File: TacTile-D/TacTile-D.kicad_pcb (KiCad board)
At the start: 2 copper layers, 60 x 60 mm, 19 parts, among them J1 Conn_01x06, J2 Conn_01x06, J3 Conn_01x06, J4 Conn_01x06, J5 Conn_01x04, J6 Conn_01x05, J7 Conn_01x02, J8 Conn_01x02, U1 74LVC2G08, U10 74LVC1G373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

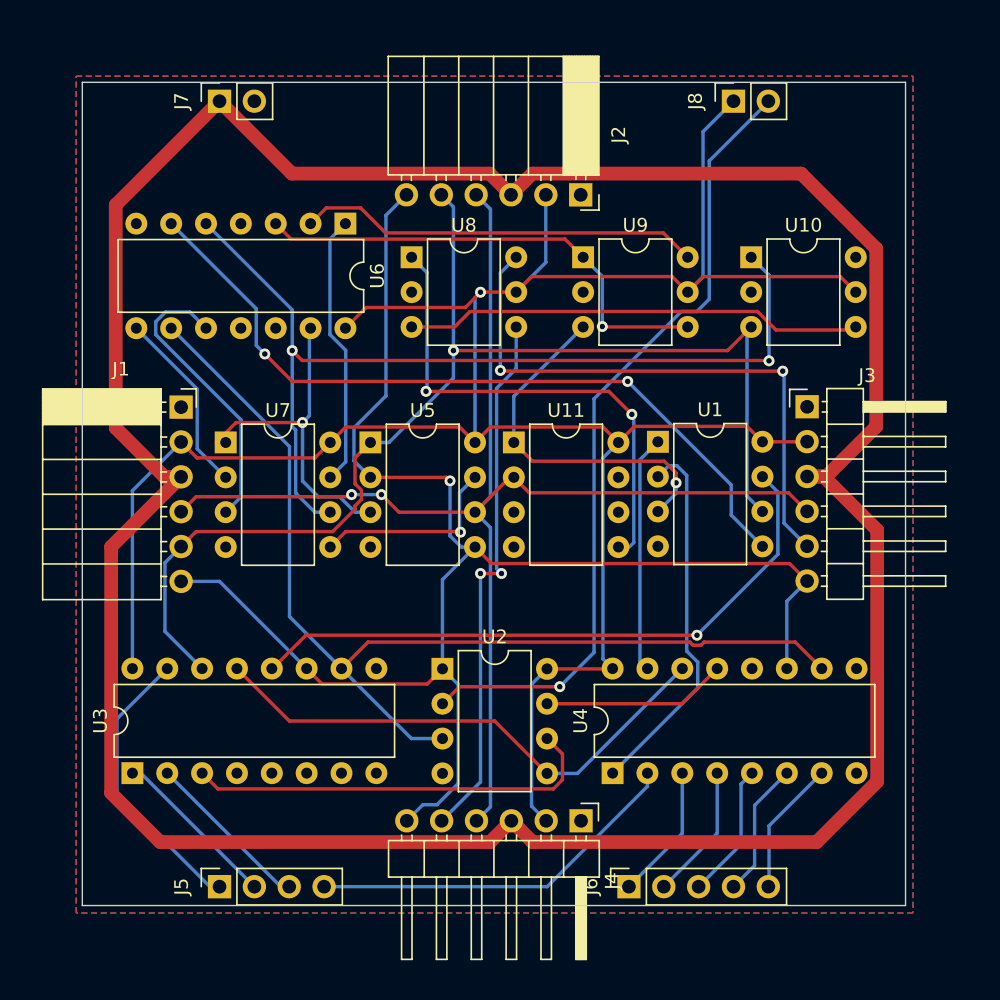
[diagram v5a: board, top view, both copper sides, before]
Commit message: Finished enlarging pins on C, D, L1, L2
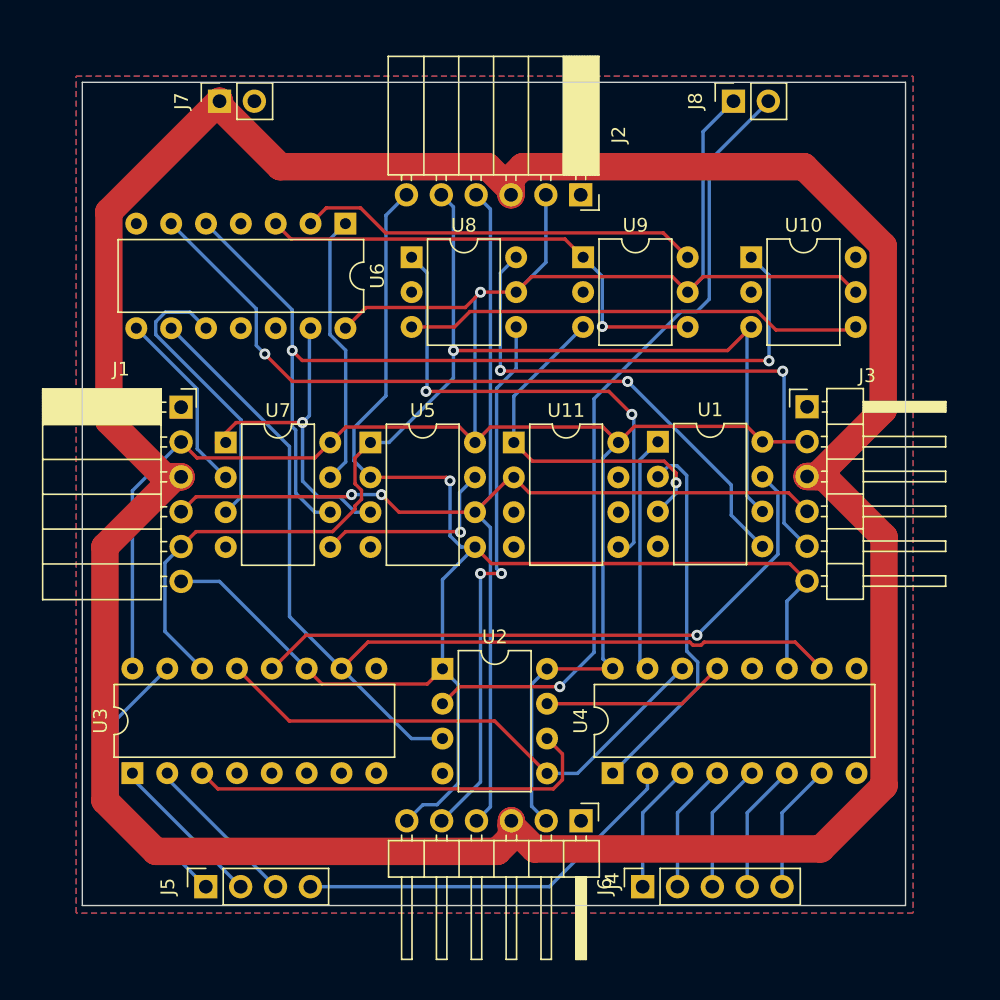
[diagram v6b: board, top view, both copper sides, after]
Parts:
- moved J5 1.00 mm to (34.0, 83.6)
- moved J6 1.00 mm to (65.8, 83.6)
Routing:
- net VIN: track 216.9 -> 223.3 mm
- net LS3: track 27.6 -> 28.7 mm
- net LS0: track 21.0 -> 20.1 mm
- net LS1: track 12.3 -> 11.5 mm
- net LS2: track 12.3 -> 11.5 mm
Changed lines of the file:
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@@
   )
   (footprint "Connector_PinSocket_2.54mm:PinSocket_1x04_P2.54mm_Vertical" (layer "F.Cu")
-    (at 35 83.625 90)
+    (at 34 83.625 90)
     (descr "Through hole straight socket strip, 1x04, 2.54mm pitch, single row (from Kicad 4.0.7), script generated")
     (tags "Through hole socket strip THT 1x04 2.54mm single row")
@@
   )
   (footprint "Connector_PinSocket_2.54mm:PinSocket_1x05_P2.54mm_Vertical" (layer "F.Cu")
-    (at 64.84 83.625 90)
+    (at 65.84 83.625 90)
     (descr "Through hole straight socket strip, 1x05, 2.54mm pitch, single row (from Kicad 4.0.7), script generated")
     (tags "Through hole socket strip THT 1x05 2.54mm single row")
@@
   (segment (start 53.73 78.825) (end 54.7455 77.8095) (width 0.25) (layer "B.Cu") (net 3))
   (segment (start 53.705 33.2) (end 54.745 34.24) (width 0.25) (layer "B.Cu") (net 3))
-  (segment (start 82.87 50.08) (end 79.22 53.73) (width 1) (layer "F.Cu") (net 4))
-  (segment (start 27.435 33.94) (end 35 26.375) (width 1) (layer "F.Cu") (net 4))
-  (segment (start 82.87 37.128679) (end 82.87 50.08) (width 1) (layer "F.Cu") (net 4))
-  (segment (start 77.825 53.73) (end 79.027081 53.73) (width 1) (layer "F.Cu") (net 4))
-  (segment (start 79.22 53.73) (end 77.825 53.73) (width 1) (layer "F.Cu") (net 4))
-  (segment (start 27.435 50.192081) (end 27.435 33.94) (width 1) (layer "F.Cu") (net 4))
-  (segment (start 56.245 33.2) (end 57.795 31.65) (width 1) (layer "F.Cu") (net 4))
-  (segment (start 54.695 31.65) (end 40.275 31.65) (width 1) (layer "F.Cu") (net 4))
-  (segment (start 54.72 80.375) (end 30.675 80.375) (width 1) (layer "F.Cu") (net 4))
-  (segment (start 57.795 31.65) (end 77.391321 31.65) (width 1) (layer "F.Cu") (net 4))
-  (segment (start 82.93 57.632919) (end 82.93 75.971321) (width 1) (layer "F.Cu") (net 4))
-  (segment (start 32.2 53.755) (end 30.997919 53.755) (width 1) (layer "F.Cu") (net 4))
-  (segment (start 56.245 33.2) (end 54.695 31.65) (width 1) (layer "F.Cu") (net 4))
-  (segment (start 79.027081 53.73) (end 82.93 57.632919) (width 1) (layer "F.Cu") (net 4))
-  (segment (start 30.675 80.375) (end 27.1 76.8) (width 1) (layer "F.Cu") (net 4))
-  (segment (start 78.526321 80.375) (end 57.82 80.375) (width 1) (layer "F.Cu") (net 4))
-  (segment (start 77.391321 31.65) (end 82.87 37.128679) (width 1) (layer "F.Cu") (net 4))
-  (segment (start 30.997919 53.755) (end 27.435 50.192081) (width 1) (layer "F.Cu") (net 4))
-  (segment (start 27.1 58.855) (end 32.2 53.755) (width 1) (layer "F.Cu") (net 4))
-  (segment (start 40.275 31.65) (end 35 26.375) (width 1) (layer "F.Cu") (net 4))
-  (segment (start 82.93 75.971321) (end 78.526321 80.375) (width 1) (layer "F.Cu") (net 4))
-  (segment (start 57.82 80.375) (end 56.27 78.825) (width 1) (layer "F.Cu") (net 4))
-  (segment (start 56.27 78.825) (end 54.72 80.375) (width 1) (layer "F.Cu") (net 4))
-  (segment (start 27.1 76.8) (end 27.1 58.855) (width 1) (layer "F.Cu") (net 4))
+  (segment (start 30.997919 53.755) (end 26.935 49.692081) (width 2) (layer "F.Cu") (net 4))
+  (segment (start 57.092919 31.15) (end 77.6 31.15) (width 2) (layer "F.Cu") (net 4))
+  (segment (start 77.6 31.15) (end 83.37 36.92) (width 2) (layer "F.Cu") (net 4))
+  (segment (start 83.37 48.88) (end 78.52 53.73) (width 2) (layer "F.Cu") (net 4))
+  (segment (start 78.52 53.73) (end 77.825 53.73) (width 2) (layer "F.Cu") (net 4))
+  (segment (start 39.415862 31.15) (end 54.554138 31.15) (width 2) (layer "F.Cu") (net 4))
+  (segment (start 78.825 80.875) (end 57.960862 80.875) (width 2) (layer "F.Cu") (net 4))
+  (segment (start 77.825 53.73) (end 79.027081 53.73) (width 2) (layer "F.Cu") (net 4))
+  (segment (start 26.65 77.35) (end 26.65 58.85) (width 2) (layer "F.Cu") (net 4))
+  (segment (start 26.65 58.85) (end 31.745 53.755) (width 2) (layer "F.Cu") (net 4))
+  (segment (start 56.27 80.027081) (end 55.247081 81.05) (width 2) (layer "F.Cu") (net 4))
+  (segment (start 56.245 32.840862) (end 56.245 33.2) (width 2) (layer "F.Cu") (net 4))
+  (segment (start 56.245 31.997919) (end 57.092919 31.15) (width 2) (layer "F.Cu") (net 4))
+  (segment (start 32.2 53.755) (end 30.997919 53.755) (width 2) (layer "F.Cu") (net 4))
+  (segment (start 79.027081 53.73) (end 83.43 58.132919) (width 2) (layer "F.Cu") (net 4))
+  (segment (start 55.247081 81.05) (end 30.35 81.05) (width 2) (layer "F.Cu") (net 4))
+  (segment (start 83.43 58.132919) (end 83.43 76.27) (width 2) (layer "F.Cu") (net 4))
+  (segment (start 35 26.734138) (end 39.415862 31.15) (width 2) (layer "F.Cu") (net 4))
+  (segment (start 83.37 36.92) (end 83.37 48.88) (width 2) (layer "F.Cu") (net 4))
+  (segment (start 57.960862 80.875) (end 56.27 79.184138) (width 2) (layer "F.Cu") (net 4))
+  (segment (start 56.27 79.184138) (end 56.27 78.825) (width 2) (layer "F.Cu") (net 4))
+  (segment (start 54.554138 31.15) (end 56.245 32.840862) (width 2) (layer "F.Cu") (net 4))
+  (segment (start 26.935 49.692081) (end 26.935 34.44) (width 2) (layer "F.Cu") (net 4))
+  (segment (start 56.245 33.2) (end 56.245 31.997919) (width 2) (layer "F.Cu") (net 4))
+  (segment (start 83.43 76.27) (end 78.825 80.875) (width 2) (layer "F.Cu") (net 4))
+  (segment (start 35 26.375) (end 35 26.734138) (width 2) (layer "F.Cu") (net 4))
+  (segment (start 31.745 53.755) (end 32.2 53.755) (width 2) (layer "F.Cu") (net 4))
+  (segment (start 30.35 81.05) (end 26.65 77.35) (width 2) (layer "F.Cu") (net 4))
+  (segment (start 56.27 78.825) (end 56.27 80.027081) (width 2) (layer "F.Cu") (net 4))
+  (segment (start 26.935 34.44) (end 35 26.375) (width 2) (layer "F.Cu") (net 4))
   (segment (start 64.07 51.25) (end 65.245 50.075) (width 0.25) (layer "F.Cu") (net 5))
   (segment (start 45.68 41.415) (end 44.175 42.92) (width 0.25) (layer "F.Cu") (net 5))
@@
   (segment (start 56.62 45.874305) (end 56.62 42.83) (width 0.25) (layer "B.Cu") (net 8))
   (segment (start 55.195 47.299305) (end 56.62 45.874305) (width 0.25) (layer "B.Cu") (net 8))
-  (segment (start 34.3 83.625) (end 27.525 76.85) (width 0.25) (layer "B.Cu") (net 9))
-  (segment (start 35.05 83.625) (end 34.3 83.625) (width 0.25) (layer "B.Cu") (net 9))
+  (segment (start 34 83.625) (end 27.525 77.15) (width 0.25) (layer "B.Cu") (net 9))
+  (segment (start 27.525 77.15) (end 27.525 71.395) (width 0.25) (layer "B.Cu") (net 9))
   (segment (start 27.525 71.395) (end 31.19 67.73) (width 0.25) (layer "B.Cu") (net 9))
-  (segment (start 27.525 76.85) (end 27.525 71.395) (width 0.25) (layer "B.Cu") (net 9))
-  (segment (start 29.265 75.35) (end 37.54 83.625) (width 0.25) (layer "B.Cu") (net 10))
-  (segment (start 28.65 75.35) (end 29.265 75.35) (width 0.25) (layer "B.Cu") (net 10))
-  (segment (start 31.19 75.35) (end 39.465 83.625) (width 0.25) (layer "B.Cu") (net 11))
-  (segment (start 39.465 83.625) (end 40.08 83.625) (width 0.25) (layer "B.Cu") (net 11))
-  (segment (start 58.875 83.625) (end 42.62 83.625) (width 0.25) (layer "B.Cu") (net 12))
-  (segment (start 66.19 76.31) (end 58.875 83.625) (width 0.25) (layer "B.Cu") (net 12))
-  (segment (start 66.19 75.35) (end 66.19 76.31) (width 0.25) (layer "B.Cu") (net 12))
-  (segment (start 68.73 75.35) (end 68.73 79.735) (width 0.25) (layer "B.Cu") (net 13))
-  (segment (start 68.73 79.735) (end 64.84 83.625) (width 0.25) (layer "B.Cu") (net 13))
-  (segment (start 71.27 75.35) (end 71.27 79.735) (width 0.25) (layer "B.Cu") (net 14))
-  (segment (start 71.27 79.735) (end 67.38 83.625) (width 0.25) (layer "B.Cu") (net 14))
-  (segment (start 73.010001 80.534999) (end 69.92 83.625) (width 0.25) (layer "B.Cu") (net 15))
-  (segment (start 73.010001 76.149999) (end 73.010001 80.534999) (width 0.25) (layer "B.Cu") (net 15))
-  (segment (start 73.81 75.35) (end 73.010001 76.149999) (width 0.25) (layer "B.Cu") (net 15))
-  (segment (start 74 82.085) (end 72.46 83.625) (width 0.25) (layer "B.Cu") (net 16))
-  (segment (start 76.35 75.35) (end 74 77.7) (width 0.25) (layer "B.Cu") (net 16))
-  (segment (start 74 77.7) (end 74 82.085) (width 0.25) (layer "B.Cu") (net 16))
-  (segment (start 75.05 83.625) (end 75.05 79.19) (width 0.25) (layer "B.Cu") (net 17))
-  (segment (start 75.05 79.19) (end 78.89 75.35) (width 0.25) (layer "B.Cu") (net 17))
+  (segment (start 36.54 83.625) (end 28.65 75.735) (width 0.25) (layer "B.Cu") (net 10))
+  (segment (start 28.65 75.735) (end 28.65 75.35) (width 0.25) (layer "B.Cu") (net 10))
+  (segment (start 39.08 83.625) (end 31.19 75.735) (width 0.25) (layer "B.Cu") (net 11))
+  (segment (start 31.19 75.735) (end 31.19 75.35) (width 0.25) (layer "B.Cu") (net 11))
+  (segment (start 66.19 76.48137) (end 66.19 75.35) (width 0.25) (layer "B.Cu") (net 12))
+  (segment (start 41.62 83.625) (end 59.04637 83.625) (width 0.25) (layer "B.Cu") (net 12))
+  (segment (start 59.04637 83.625) (end 66.19 76.48137) (width 0.25) (layer "B.Cu") (net 12))
+  (segment (start 65.84 78.24) (end 68.73 75.35) (width 0.25) (layer "B.Cu") (net 13))
+  (segment (start 65.84 83.625) (end 65.84 78.24) (width 0.25) (layer "B.Cu") (net 13))
+  (segment (start 68.38 83.625) (end 68.38 78.24) (width 0.25) (layer "B.Cu") (net 14))
+  (segment (start 68.38 78.24) (end 71.27 75.35) (width 0.25) (layer "B.Cu") (net 14))
+  (segment (start 70.92 78.24) (end 73.81 75.35) (width 0.25) (layer "B.Cu") (net 15))
+  (segment (start 70.92 83.625) (end 70.92 78.24) (width 0.25) (layer "B.Cu") (net 15))
+  (segment (start 73.46 78.24) (end 76.35 75.35) (width 0.25) (layer "B.Cu") (net 16))
+  (segment (start 73.46 83.625) (end 73.46 78.24) (width 0.25) (layer "B.Cu") (net 16))
+  (segment (start 76 83.625) (end 76 78.24) (width 0.25) (layer "B.Cu") (net 17))
+  (segment (start 76 78.24) (end 78.89 75.35) (width 0.25) (layer "B.Cu") (net 17))
   (segment (start 52.49 69.05) (end 51.25 70.29) (width 0.25) (layer "F.Cu") (net 18))
   (segment (start 59.8 69.05) (end 52.49 69.05) (width 0.25) (layer "F.Cu") (net 18))

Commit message: Checked new board D spacing requirements
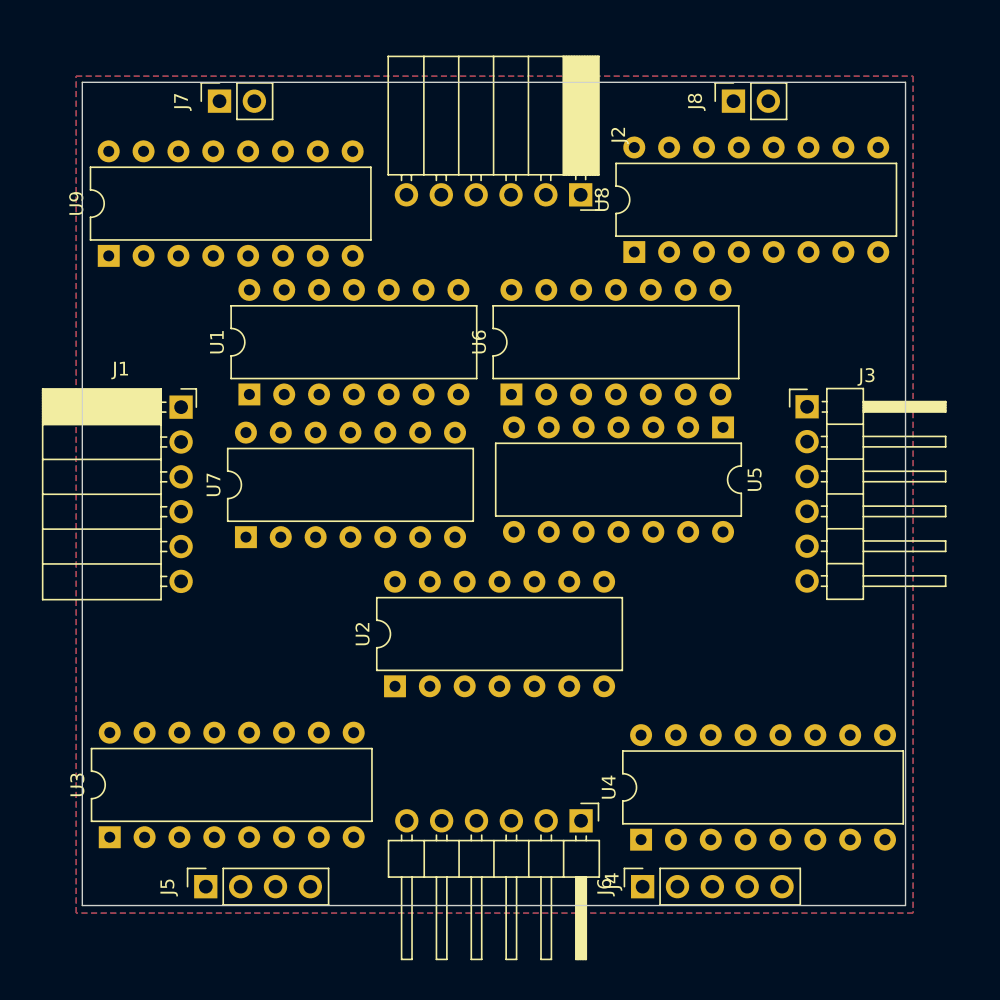
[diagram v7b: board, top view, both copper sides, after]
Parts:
- removed U10: 74LVC1G373, Package_DIP:DIP-6_W7.62mm
- removed U11: 74AUC1G74, Package_DIP:DIP-8_W7.62mm
- removed the U5 at (46.0, 51.2)
- added U6: 74HC08, Package_DIP:DIP-14_W7.62mm, F.Cu at (56.3, 47.8)
- U1: value 74LVC2G08 -> 74LS04; footprint Package_DIP:DIP-8_W7.62mm -> Package_DIP:DIP-14_W7.62mm
- U2: value 74LVC3G04 -> 4011; footprint Package_DIP:DIP-8_W7.62mm -> Package_DIP:DIP-14_W7.62mm
- U7: value 74LVC2G32 -> 74LS74; footprint Package_DIP:DIP-8_W7.62mm -> Package_DIP:DIP-14_W7.62mm
- U8: value 74LVC1G18 -> 4042; footprint Package_DIP:DIP-6_W7.62mm -> Package_DIP:DIP-16_W7.62mm
- U9: value 74LVC2G04 -> 74HC4051; footprint Package_DIP:DIP-6_W7.62mm -> Package_DIP:DIP-16_W7.62mm
- moved U9 34.6 mm to (26.9, 37.6), turned to 90 degrees
- moved U5 31.3 mm to (71.7, 50.1)
- moved U1 30.0 mm to (37.2, 47.8), turned to 90 degrees
- moved U8 16.2 mm to (65.2, 37.4), turned to 90 degrees
- moved U7 7.06 mm to (36.9, 58.1), turned to 90 degrees
- moved U4 5.28 mm to (65.7, 80.2)
- moved U3 4.95 mm to (27.0, 80.0)
- moved U2 3.69 mm to (47.8, 69.0), turned to 90 degrees
- renumbered U6 to U5
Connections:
- U1 pad 1: Net-(U4-Q0) -> CLK
- U1 pad 2: Net-(U4-Q1) -> Net-(U4-CPR)
- U1 pad 3: Net-(U11-C) -> SEN
- U1 pad 4: GND -> Net-(U3-~{OE})
- U1 pad 5: Net-(U6A-~{Q}) -> Net-(U3-QD)
- U1 pad 6: MOSI -> LEN
- U1 pad 7: Net-(U3-RCLK) -> GND
- U1 pad 8: VCC -> Net-(U5A-D)
- U2 pad 2: LEN -> SS
- U2 pad 3: SEN -> Net-(U5B-~{R})
- U2 pad 4: GND -> Net-(U5B-~{S})
- U2 pad 5: Net-(U3-~{OE}) -> Net-(U2-Pad5)
- U2 pad 6: Net-(U3-QD) -> Net-(U5A-~{Q})
- U2 pad 7: Net-(U4-CPR) -> GND
- U2 pad 8: VCC -> Net-(U5A-~{Q})
- U5 pad 1: Net-(U6A-~{R}) -> Net-(U5A-~{R})
- U5 pad 10: Net-(U6B-~{S}) -> Net-(U5B-~{S})
- U5 pad 13: Net-(U6B-~{R}) -> Net-(U5B-~{R})
- U5 pad 2: Net-(U6A-D) -> Net-(U5A-D)
- U5 pad 3: Net-(U6A-C) -> Net-(U5A-C)
- U5 pad 4: GND -> VCC
- U5 pad 5: Net-(U10-LE) -> Net-(U5A-Q)
- U5 pad 6: Net-(U6A-~{Q}) -> Net-(U5A-~{Q})
- U5 pad 8: Net-(U6B-~{Q}) -> Net-(U5B-~{Q})
- U7 pad 1: Net-(U6B-~{R}) -> VCC
- U7 pad 2: Net-(U6B-~{Q}) -> SS
- U7 pad 3: Net-(U6B-~{S}) -> Net-(U7A-C)
- U7 pad 4: GND -> VCC
- U7 pad 5: Net-(U5-Pad7) -> Net-(U7A-Q)
- U7 pad 6: Net-(U10-LE) -> unconnected-(U7A-~{Q}-Pad6)
- U7 pad 7: Net-(U6A-~{R}) -> GND
- U7 pad 8: VCC -> (no net)
- U8 pad 1: Net-(U11-Q) -> unconnected-(U8-Pad1)
- U8 pad 2: GND -> Net-(U9-A)
- U8 pad 3: Net-(U10-Q) -> unconnected-(U8-Pad3)
- U8 pad 4: MISO1 -> MOSI
- U8 pad 5: VCC -> Net-(U5A-Q)
- U8 pad 6: MISO0 -> VCC
- U9 pad 1: Net-(U6A-C) -> unconnected-(U9-A4-Pad1)
- U9 pad 2: GND -> unconnected-(U9-A6-Pad2)
- U9 pad 3: Net-(U11-C) -> Net-(U9-A)
- U9 pad 4: Net-(U6A-C) -> unconnected-(U9-A7-Pad4)
- U9 pad 5: VCC -> unconnected-(U9-A5-Pad5)
- U9 pad 6: Net-(U6A-D) -> GND
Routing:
- net VIN: track 223.3 -> 0.00 mm
- net VCC: track 175.9 -> 0.00 mm, vias 1 -> 0
- net CLK: track 113.1 -> 0.00 mm, vias 1 -> 0
- net SS: track 96.2 -> 0.00 mm, vias 2 -> 0
- net MOSI: track 88.8 -> 0.00 mm, vias 1 -> 0
- net SEN: track 76.2 -> 0.00 mm
- net Net-(U10-LE): track 68.6 -> 0.00 mm, vias 2 -> 0
- net LEN: track 58.7 -> 0.00 mm, vias 1 -> 0
- net Net-(U6A-~{Q}): track 55.7 -> 0.00 mm, vias 2 -> 0
- net Net-(U3-RCLK): track 46.5 -> 0.00 mm, vias 1 -> 0
- net MISO0: track 42.8 -> 0.00 mm, vias 2 -> 0
- net MISO1: track 39.4 -> 0.00 mm, vias 2 -> 0
- net Net-(U3-~{OE}): track 38.8 -> 0.00 mm
- net Net-(U11-Q): track 35.8 -> 0.00 mm, vias 2 -> 0
- net Net-(U6A-C): track 35.3 -> 0.00 mm, vias 1 -> 0
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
